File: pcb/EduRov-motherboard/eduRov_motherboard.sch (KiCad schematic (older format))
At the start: 25 parts, among them P101 Battery connector, P102 Ext press, P103 Ext temp, Q101 IRL540NPBF

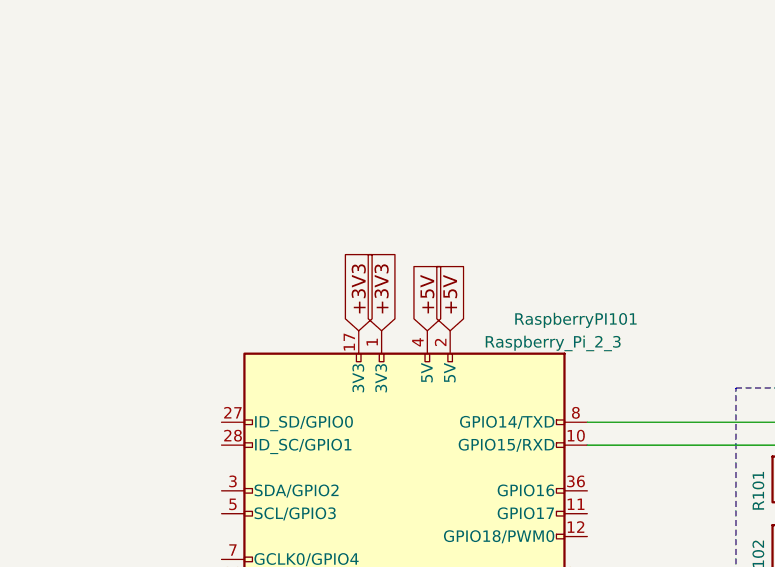
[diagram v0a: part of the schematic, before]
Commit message: Update PCBs from testing of first prototype.
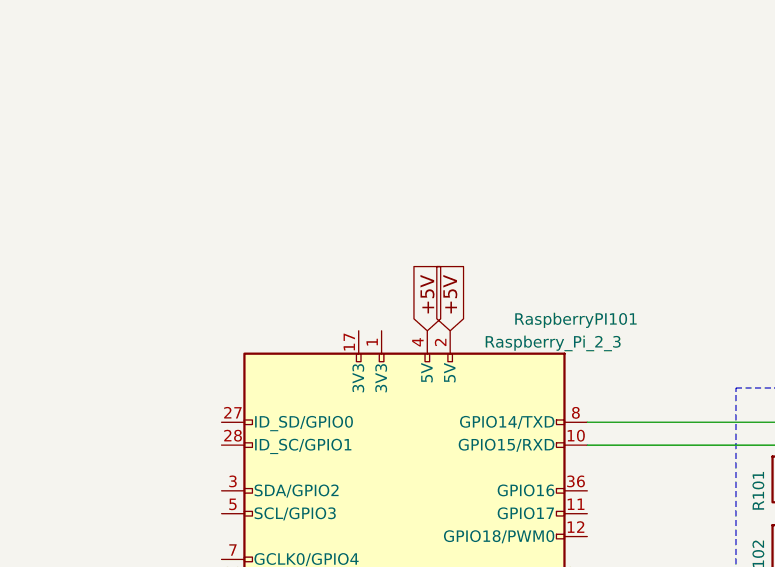
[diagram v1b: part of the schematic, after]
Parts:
- R101, R102, R103, R104, R108, R109, R110, R111: footprint Resistor_THT:R_Axial_DIN0204_L3.6mm_D1.6mm_P7.62mm_Horizontal -> Resistor_THT:R_Axial_DIN0207_L6.3mm_D2.5mm_P10.16mm_Horizontal
- R105, R107: footprint Resistors_THT:R_Axial_DIN0204_L3.6mm_D1.6mm_P7.62mm_Horizontal -> Resistor_THT:R_Axial_DIN0207_L6.3mm_D2.5mm_P10.16mm_Horizontal
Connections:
- net labels removed: +3V3
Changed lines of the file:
@@
 F 0 "R110" V 14630 5050 50  0000 C CNN
 F 1 "10k" V 14550 5050 50  0000 C CNN
-F 2 "Resistor_THT:R_Axial_DIN0204_L3.6mm_D1.6mm_P7.62mm_Horizontal" V 14480 5050 50  0001 C CNN
+F 2 "Resistor_THT:R_Axial_DIN0207_L6.3mm_D2.5mm_P10.16mm_Horizontal" V 14480 5050 50  0001 C CNN
 F 3 "" H 14550 5050 50  0000 C CNN
 	1    14550 5050
@@
 F 0 "R107" V 14230 7650 50  0000 C CNN
 F 1 "10k" V 14150 7650 50  0000 C CNN
-F 2 "Resistors_THT:R_Axial_DIN0204_L3.6mm_D1.6mm_P7.62mm_Horizontal" V 14080 7650 50  0001 C CNN
+F 2 "Resistor_THT:R_Axial_DIN0207_L6.3mm_D2.5mm_P10.16mm_Horizontal" V 14080 7650 50  0001 C CNN
 F 3 "" H 14150 7650 50  0000 C CNN
 	1    14150 7650
@@
 F 0 "R111" V 14630 5350 50  0000 C CNN
 F 1 "10k" V 14550 5350 50  0000 C CNN
-F 2 "Resistor_THT:R_Axial_DIN0204_L3.6mm_D1.6mm_P7.62mm_Horizontal" V 14480 5350 50  0001 C CNN
+F 2 "Resistor_THT:R_Axial_DIN0207_L6.3mm_D2.5mm_P10.16mm_Horizontal" V 14480 5350 50  0001 C CNN
 F 3 "" H 14550 5350 50  0000 C CNN
 	1    14550 5350
@@
 F 0 "R109" V 14630 4750 50  0000 C CNN
 F 1 "10k" V 14550 4750 50  0000 C CNN
-F 2 "Resistor_THT:R_Axial_DIN0204_L3.6mm_D1.6mm_P7.62mm_Horizontal" V 14480 4750 50  0001 C CNN
+F 2 "Resistor_THT:R_Axial_DIN0207_L6.3mm_D2.5mm_P10.16mm_Horizontal" V 14480 4750 50  0001 C CNN
 F 3 "" H 14550 4750 50  0000 C CNN
 	1    14550 4750
@@
 F 0 "R105" V 5780 4750 50  0000 C CNN
 F 1 "10k" V 5700 4750 50  0000 C CNN
-F 2 "Resistors_THT:R_Axial_DIN0204_L3.6mm_D1.6mm_P7.62mm_Horizontal" V 5630 4750 50  0001 C CNN
+F 2 "Resistor_THT:R_Axial_DIN0207_L6.3mm_D2.5mm_P10.16mm_Horizontal" V 5630 4750 50  0001 C CNN
 F 3 "" H 5700 4750 50  0000 C CNN
 	1    5700 4750
@@
 F 0 "R108" V 14630 4450 50  0000 C CNN
 F 1 "10k" V 14550 4450 50  0000 C CNN
-F 2 "Resistor_THT:R_Axial_DIN0204_L3.6mm_D1.6mm_P7.62mm_Horizontal" V 14480 4450 50  0001 C CNN
+F 2 "Resistor_THT:R_Axial_DIN0207_L6.3mm_D2.5mm_P10.16mm_Horizontal" V 14480 4450 50  0001 C CNN
 F 3 "" H 14550 4450 50  0000 C CNN
 	1    14550 4450
@@
 Wire Notes Line
 	6800 3950 6800 3350
-Text GLabel 2250 3950 1    60   Input ~ 0
-+3V3
-Text GLabel 2350 3950 1    60   Input ~ 0
-+3V3
 $Comp
 L Device:C C107
@@
 F 0 "R102" V 4000 4950 50  0000 C CNN
 F 1 "10k" V 4100 4900 50  0000 C CNN
-F 2 "Resistor_THT:R_Axial_DIN0204_L3.6mm_D1.6mm_P7.62mm_Horizontal" V 4030 4900 50  0001 C CNN
+F 2 "Resistor_THT:R_Axial_DIN0207_L6.3mm_D2.5mm_P10.16mm_Horizontal" V 4030 4900 50  0001 C CNN
 F 3 "" H 4100 4900 50  0000 C CNN
 	1    4100 4900
@@
 F 0 "R101" V 4000 4650 50  0000 C CNN
 F 1 "10k" V 4100 4600 50  0000 C CNN
-F 2 "Resistor_THT:R_Axial_DIN0204_L3.6mm_D1.6mm_P7.62mm_Horizontal" V 4030 4600 50  0001 C CNN
+F 2 "Resistor_THT:R_Axial_DIN0207_L6.3mm_D2.5mm_P10.16mm_Horizontal" V 4030 4600 50  0001 C CNN
 F 3 "" H 4100 4600 50  0000 C CNN
 	1    4100 4600
@@
 F 0 "R103" V 4300 4550 50  0000 C CNN
 F 1 "10k" V 4250 4350 50  0000 C CNN
-F 2 "Resistor_THT:R_Axial_DIN0204_L3.6mm_D1.6mm_P7.62mm_Horizontal" V 4180 4350 50  0001 C CNN
+F 2 "Resistor_THT:R_Axial_DIN0207_L6.3mm_D2.5mm_P10.16mm_Horizontal" V 4180 4350 50  0001 C CNN
 F 3 "" H 4250 4350 50  0000 C CNN
 	1    4250 4350
@@
 F 0 "R104" V 4200 4250 50  0000 C CNN
 F 1 "10k" V 4250 4450 50  0000 C CNN
-F 2 "Resistor_THT:R_Axial_DIN0204_L3.6mm_D1.6mm_P7.62mm_Horizontal" V 4180 4450 50  0001 C CNN
+F 2 "Resistor_THT:R_Axial_DIN0207_L6.3mm_D2.5mm_P10.16mm_Horizontal" V 4180 4450 50  0001 C CNN
 F 3 "" H 4250 4450 50  0000 C CNN
 	1    4250 4450

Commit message: Update PCBs after prototyping
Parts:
- removed P103: Ext temp, Connectors_Terminal_Blocks:TerminalBlock_Altech_AK300-3_P5.00mm, symbol eduROV_motherboard:CONN_01X03-eduRov_motherboard-rescue
- added P103: Ext press, Connector_JST:JST_PH_B3B-PH-K_1x03_P2.00mm_Vertical, symbol Connector_Generic:Conn_01x03
- added P104: Ext press, Connector_JST:JST_PH_B4B-PH-K_1x04_P2.00mm_Vertical, symbol Connector_Generic:Conn_01x04
- 2Pscrew101, 2Pscrew102, 2Pscrew103, 2Pscrew104: footprint Connectors_Terminal_Blocks:TerminalBlock_Altech_AK300-2_P5.00mm -> TerminalBlock_Altech:Altech_AK300_1x02_P5.00mm_45-Degree; symbol eduROV_motherboard:CONN_01X02-eduRov_motherboard-rescue -> Connector_Generic:Conn_01x02
- P101: symbol eduROV_motherboard:CONN_01X02-eduRov_motherboard-rescue -> Connector_Generic:Conn_01x02
- P102: footprint Connectors_Terminal_Blocks:TerminalBlock_Altech_AK300-3_P5.00mm -> Connector_JST:JST_PH_B3B-PH-K_1x03_P2.00mm_Vertical; symbol eduROV_motherboard:CONN_01X03-eduRov_motherboard-rescue -> Connector_Generic:Conn_01x03
- P105: renamed from 2Pscrew105; footprint Connectors_Terminal_Blocks:TerminalBlock_Altech_AK300-2_P5.00mm -> Connector_JST:JST_PH_B4B-PH-K_1x04_P2.00mm_Vertical; symbol eduROV_motherboard:CONN_01X02-eduRov_motherboard-rescue -> Connector_Generic:Conn_01x04
- Q101: footprint TO_SOT_Packages_THT:TO-220-3_Vertical -> Package_TO_SOT_THT:TO-220-3_Vertical; symbol eduROV_motherboard:IRL540NPBF-eduRov_motherboard-rescue -> EduROV:IRL540NPBF
- renumbered C107 to C102
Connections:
- net labels added: +3V3, SCL, SDA
- wire segments 52 -> 57
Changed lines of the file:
@@
 +Bat1
 $Comp
-L eduROV_motherboard:CONN_01X03-eduRov_motherboard-rescue P103
-U 1 1 59CD072D
-P 14850 6400
-F 0 "P103" H 14850 6600 50  0000 C CNN
-F 1 "Ext temp" V 14950 6400 50  0000 C CNN
-F 2 "Connectors_Terminal_Blocks:TerminalBlock_Altech_AK300-3_P5.00mm" H 14850 6400 50  0001 C CNN
-F 3 "" H 14850 6400 50  0000 C CNN
-	1    14850 6400
-	1    0    0    -1
-$EndComp
-$Comp
-L eduROV_motherboard:CONN_01X03-eduRov_motherboard-rescue P102
+L Connector_Generic:Conn_01x03 P102
 U 1 1 59CD089E
 P 14850 5950
 F 0 "P102" H 14850 6150 50  0000 C CNN
 F 1 "Ext press" V 14950 5950 50  0000 C CNN
-F 2 "Connectors_Terminal_Blocks:TerminalBlock_Altech_AK300-3_P5.00mm" H 14850 5950 50  0001 C CNN
+F 2 "Connector_JST:JST_PH_B3B-PH-K_1x03_P2.00mm_Vertical" H 14850 5950 50  0001 C CNN
 F 3 "" H 14850 5950 50  0000 C CNN
 	1    14850 5950
@@
 PressMonitor
 $Comp
-L eduROV_motherboard:CONN_01X02-eduRov_motherboard-rescue 2Pscrew103
+L Connector_Generic:Conn_01x02 2Pscrew103
 U 1 1 59CD3D3E
-P 12600 4700
-F 0 "2Pscrew103" H 12950 4650 50  0000 C CNN
-F 1 "Channel 3" H 12900 4750 50  0000 C CNN
-F 2 "Connectors_Terminal_Blocks:TerminalBlock_Altech_AK300-2_P5.00mm" H 12600 4700 50  0001 C CNN
-F 3 "" H 12600 4700 50  0000 C CNN
-	1    12600 4700
-	1    0    0    -1
+P 12600 4750
+F 0 "2Pscrew103" H 12950 4700 50  0000 C CNN
+F 1 "Channel 3" H 12900 4800 50  0000 C CNN
+F 2 "TerminalBlock_Altech:Altech_AK300_1x02_P5.00mm_45-Degree" H 12600 4750 50  0001 C CNN
+F 3 "" H 12600 4750 50  0000 C CNN
+	1    12600 4750
+	1    0    0    1
 $EndComp
 Text GLabel 13950 7500 0    60   Input ~ 0
@@
 GND
 $Comp
-L eduROV_motherboard:CONN_01X02-eduRov_motherboard-rescue 2Pscrew105
+L Connector_Generic:Conn_01x04 P105
 U 1 1 59D3A8DC
-P 15000 8050
-F 0 "2Pscrew105" H 15000 8200 50  0000 C CNN
-F 1 "Ch LED" V 15100 8050 50  0000 C CNN
-F 2 "Connectors_Terminal_Blocks:TerminalBlock_Altech_AK300-2_P5.00mm" H 15000 8050 50  0001 C CNN
-F 3 "" H 15000 8050 50  0000 C CNN
-	1    15000 8050
+P 15250 7900
+F 0 "P105" H 15275 8100 50  0000 C CNN
+F 1 "Ch LED" V 15350 7900 50  0000 C CNN
+F 2 "Connector_JST:JST_PH_B4B-PH-K_1x04_P2.00mm_Vertical" H 15250 7900 50  0001 C CNN
+F 3 "" H 15250 7900 50  0000 C CNN
+	1    15250 7900
 	1    0    0    -1
 $EndComp
@@
 +Bat1
 $Comp
-L eduROV_motherboard:CONN_01X02-eduRov_motherboard-rescue P101
+L Connector_Generic:Conn_01x02 P101
 U 1 1 59F0943E
 P 1350 1100
@@
 $EndComp
 $Comp
-L eduROV_motherboard:IRL540NPBF-eduRov_motherboard-rescue Q101
+L EduROV:IRL540NPBF Q101
 U 1 1 5A60C2A4
 P 14600 7700
 F 0 "Q101" H 14850 7775 50  0000 L CNN
 F 1 "IRL540NPBF" H 14850 7700 50  0001 L CNN
-F 2 "TO_SOT_Packages_THT:TO-220-3_Vertical" H 14850 7625 50  0001 L CIN
+F 2 "Package_TO_SOT_THT:TO-220-3_Vertical" H 14850 7625 50  0001 L CIN
 F 3 "" H 14600 7700 50  0001 L CNN
 	1    14600 7700
@@
 Connection ~ 14150 8100
 Wire Wire Line
-	14150 8100 14800 8100
-Wire Wire Line
 	13950 7800 14150 7800
 Connection ~ 14150 7800
@@
 Mot3-
 $Comp
-L eduROV_motherboard:CONN_01X02-eduRov_motherboard-rescue 2Pscrew102
-U 1 1 59CCD414
-P 12600 3500
-F 0 "2Pscrew102" H 12950 3450 50  0000 C CNN
-F 1 "Channel 2" H 12900 3550 50  0000 C CNN
-F 2 "Connectors_Terminal_Blocks:TerminalBlock_Altech_AK300-2_P5.00mm" H 12600 3500 50  0001 C CNN
-F 3 "" H 12600 3500 50  0000 C CNN
-	1    12600 3500
-	1    0    0    -1
-$EndComp
-$Comp
-L eduROV_motherboard:CONN_01X02-eduRov_motherboard-rescue 2Pscrew101
+L Connector_Generic:Conn_01x02 2Pscrew101
 U 1 1 59CD3B58
-P 12600 2350
-F 0 "2Pscrew101" H 12950 2300 50  0000 C CNN
-F 1 "Channel 1" H 12900 2400 50  0000 C CNN
-F 2 "Connectors_Terminal_Blocks:TerminalBlock_Altech_AK300-2_P5.00mm" H 12600 2350 50  0001 C CNN
-F 3 "" H 12600 2350 50  0000 C CNN
-	1    12600 2350
-	1    0    0    -1
+P 12600 2400
+F 0 "2Pscrew101" H 12950 2350 50  0000 C CNN
+F 1 "Channel 1" H 12900 2450 50  0000 C CNN
+F 2 "TerminalBlock_Altech:Altech_AK300_1x02_P5.00mm_45-Degree" H 12600 2400 50  0001 C CNN
+F 3 "" H 12600 2400 50  0000 C CNN
+	1    12600 2400
+	1    0    0    1
 $EndComp
 $Sheet
@@
 +Bat1
 $Comp
-L eduROV_motherboard:CONN_01X02-eduRov_motherboard-rescue 2Pscrew104
+L Connector_Generic:Conn_01x02 2Pscrew104
 U 1 1 59CD3CF4
-P 12600 5900
-F 0 "2Pscrew104" H 12950 5850 50  0000 C CNN
-F 1 "Channel 4" H 12900 5950 50  0000 C CNN
-F 2 "Connectors_Terminal_Blocks:TerminalBlock_Altech_AK300-2_P5.00mm" H 12600 5900 50  0001 C CNN
-F 3 "" H 12600 5900 50  0000 C CNN
-	1    12600 5900
-	1    0    0    -1
+P 12600 5950
+F 0 "2Pscrew104" H 12950 5900 50  0000 C CNN
+F 1 "Channel 4" H 12900 6000 50  0000 C CNN
+F 2 "TerminalBlock_Altech:Altech_AK300_1x02_P5.00mm_45-Degree" H 12600 5950 50  0001 C CNN
+F 3 "" H 12600 5950 50  0000 C CNN
+	1    12600 5950
+	1    0    0    1
 $EndComp
 Wire Wire Line
@@
 	6800 3950 6800 3350
 $Comp
-L Device:C C107
+L Device:C C102
 U 1 1 5FC68142
 P 14150 7950
-F 0 "C107" H 14400 7900 50  0000 R CNN
+F 0 "C102" H 14400 7900 50  0000 R CNN
 F 1 "100nF" H 14500 8000 50  0000 R CNN
 F 2 "Capacitor_THT:C_Disc_D5.0mm_W2.5mm_P2.50mm" H 14188 7800 50  0001 C CNN
@@
 Wire Wire Line
 	6250 4350 4400 4350
+$Comp
+L Connector_Generic:Conn_01x03 P103
+U 1 1 60763419
+P 14850 6400
+F 0 "P103" H 14850 6600 50  0000 C CNN
+F 1 "Ext press" V 14950 6400 50  0000 C CNN
+F 2 "Connector_JST:JST_PH_B3B-PH-K_1x03_P2.00mm_Vertical" H 14850 6400 50  0001 C CNN
+F 3 "" H 14850 6400 50  0000 C CNN
+	1    14850 6400
+	1    0    0    -1
+$EndComp
+$Comp
+L Connector_Generic:Conn_01x04 P104
+U 1 1 60771AD7
+P 14850 6850
+F 0 "P104" H 14850 7050 50  0000 C CNN
+F 1 "Ext press" V 14950 6850 50  0000 C CNN
+F 2 "Connector_JST:JST_PH_B4B-PH-K_1x04_P2.00mm_Vertical" H 14850 6850 50  0001 C CNN
+F 3 "" H 14850 6850 50  0000 C CNN
+	1    14850 6850
+	1    0    0    -1
+$EndComp
+Text GLabel 14650 7050 0    60   Input ~ 0
+GND
+Text GLabel 14650 6950 0    60   Input ~ 0
+SCL
+Text GLabel 14650 6750 0    60   Input ~ 0
++3V3
+Text GLabel 14650 6850 0    60   Input ~ 0
+SDA
+Text GLabel 1650 4650 0    60   Input ~ 0
+SCL
+Text GLabel 1650 4750 0    60   Input ~ 0
+SDA
+Text GLabel 2250 3950 1    60   Input ~ 0
++3V3
+Text GLabel 2350 3950 1    60   Input ~ 0
++3V3
+$Comp
+L Connector_Generic:Conn_01x02 2Pscrew102
+U 1 1 59CCD414
+P 12600 3550
+F 0 "2Pscrew102" H 12950 3500 50  0000 C CNN
+F 1 "Channel 2" H 12900 3600 50  0000 C CNN
+F 2 "TerminalBlock_Altech:Altech_AK300_1x02_P5.00mm_45-Degree" H 12600 3550 50  0001 C CNN
+F 3 "" H 12600 3550 50  0000 C CNN
+	1    12600 3550
+	1    0    0    1
+$EndComp
+Wire Wire Line
+	15050 7900 14875 7900
+Wire Wire Line
+	14875 7900 14875 8100
+Wire Wire Line
+	14150 8100 14875 8100
+Wire Wire Line
+	14875 8100 15050 8100
+Connection ~ 14875 8100
+Wire Wire Line
+	15050 8000 14800 8000
+Wire Wire Line
+	14800 7800 15050 7800
+Connection ~ 14800 7800
 $EndSCHEMATC

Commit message: Update library use.
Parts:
- Q101: symbol EduROV:IRL540NPBF -> Edurov:IRL540NPBF
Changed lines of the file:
@@
 $EndComp
 $Comp
-L EduROV:IRL540NPBF Q101
+L Edurov:IRL540NPBF Q101
 U 1 1 5A60C2A4
 P 14600 7700

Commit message: Update schematic.
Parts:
- removed R106: 0, Resistor_THT:R_Axial_DIN0204_L3.6mm_D1.6mm_P1.90mm_Vertical, symbol Device:R
- RaspberryPI101: footprint EduROV:RaspBerry_PI -> EduRov:RaspBerry_PI
- renumbered R107 to R112
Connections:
- net labels added: LED-
- wire segments 57 -> 63
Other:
- note added: "Actuators"
- note added: "Battery level"
- note added: "Computing"
- note added: "Headlights"
- note added: "I2C bus"
- note added: "Power in\n"
- note added: "Pressure"
- note added: "Sensor connectors compatible with Adafruit Stemma system."
- note added: "Sensors"
- note added: "Temperature"
- note removed: "Connects Arduino 5V to board 5V.\nDo not connect this if using \nUSB to power Arduino."
- moved on the sheet: 2Pscrew101, 2Pscrew102, 2Pscrew103, 2Pscrew104, 5vReg101, A101, C101, C102, P101, P102, P103, P104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
